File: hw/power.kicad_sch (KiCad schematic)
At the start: 2 parts, among them J1 TYPE-C-31-M-13C

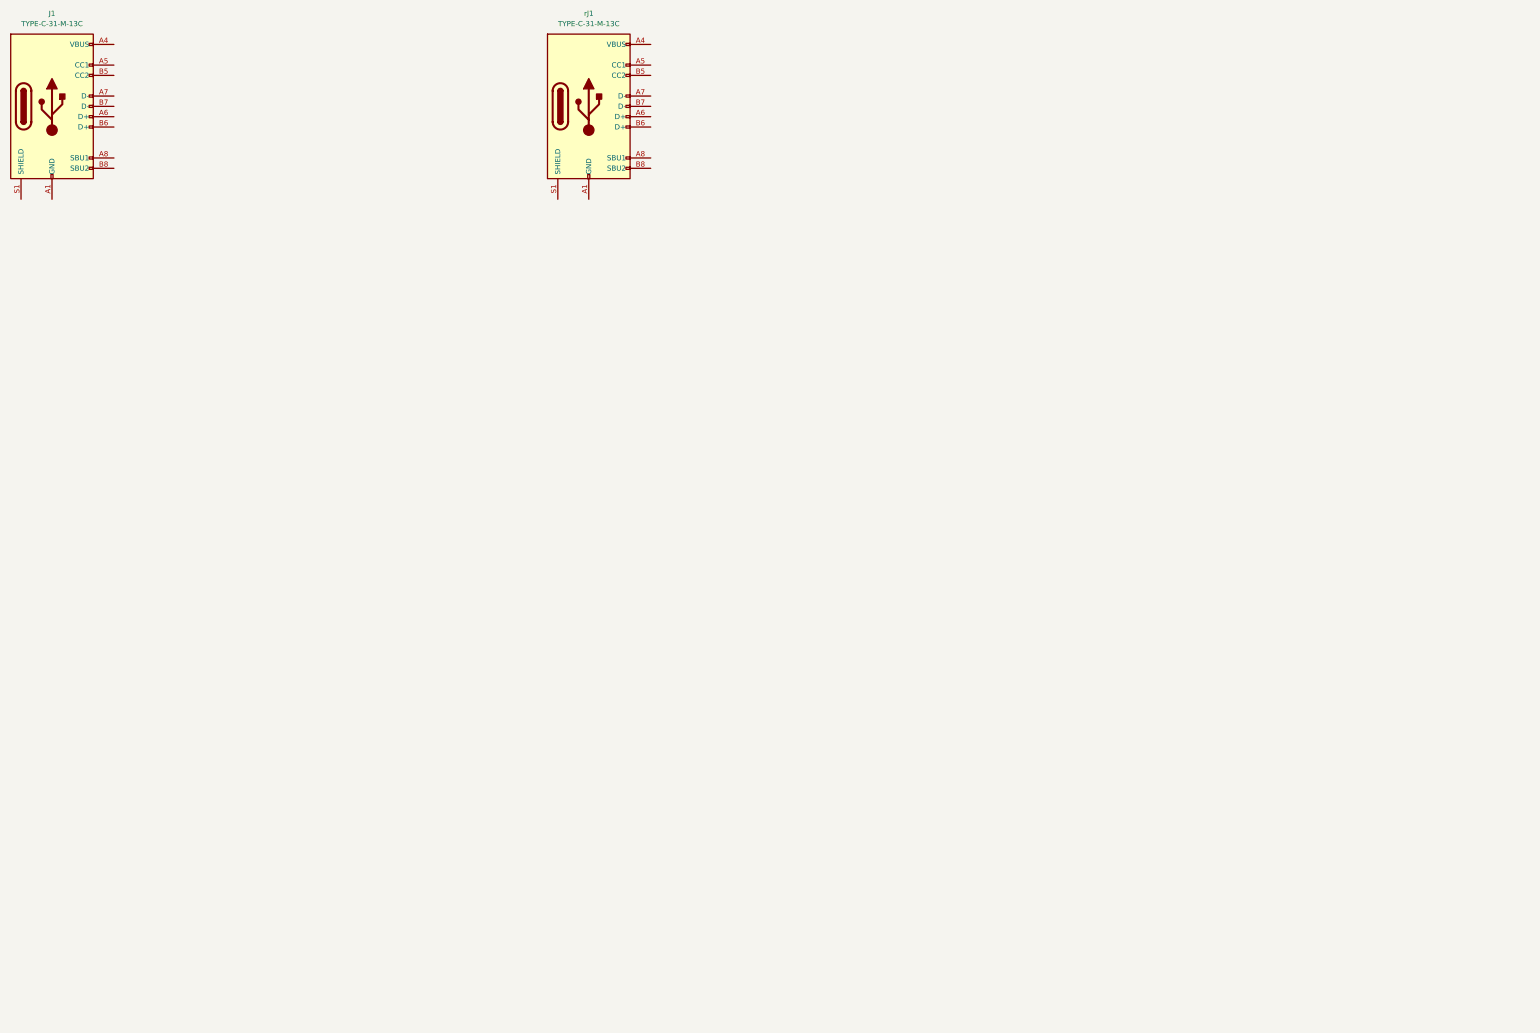
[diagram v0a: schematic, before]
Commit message: Power schematic with npm1100 setup
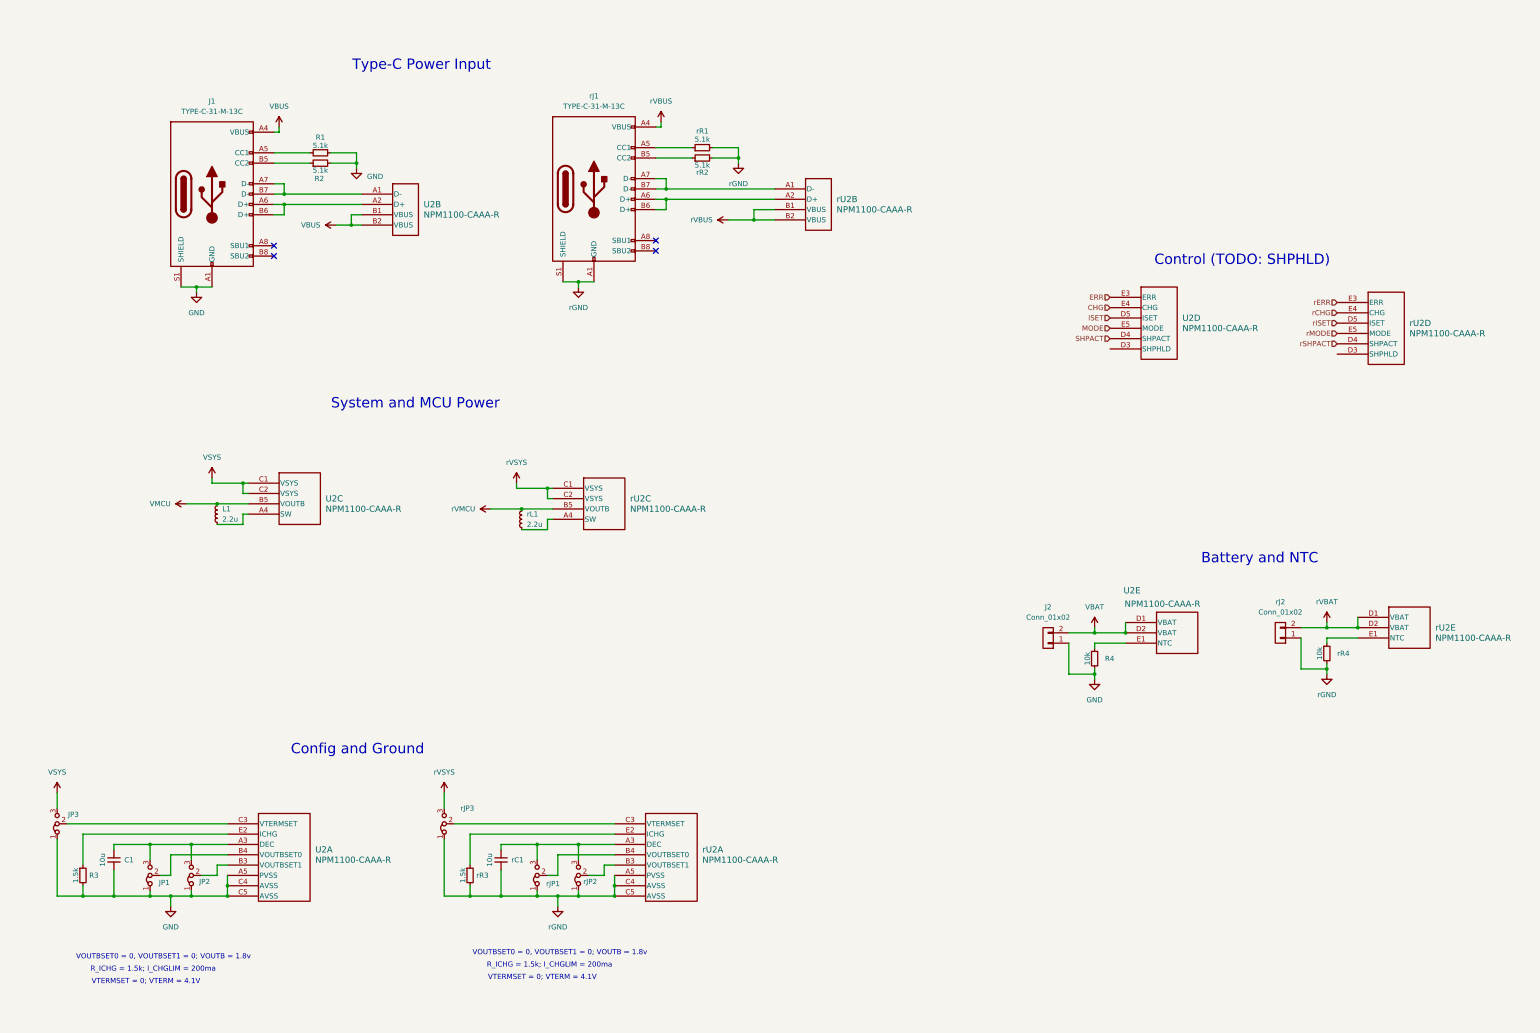
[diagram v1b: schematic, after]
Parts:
- added C1, rC1: 10u, symbol Alidade:C
- added J2, rJ2: Conn_01x02, symbol Alidade:Conn_01x02
- added JP1, JP2, JP3, rJP1, rJP2, rJP3: Jumper_3_Bridged12, symbol Alidade:Jumper_3_Bridged12
- added L1, rL1: 2.2u, symbol Alidade:L
- added R1, R2, rR1, rR2: 5.1k, symbol Alidade:R
- added R3, rR3: 1.5k, symbol Alidade:R
- added R4, rR4: 10k, symbol Alidade:R
- added U2, rU2: NPM1100-CAAA-R, Alidade:WLCSP_2p075X2p075_NOR, symbol Alidade:NPM1100-CAAA-R
- J1, rJ1: symbol Connector:USB_C_Receptacle_USB2.0 -> Alidade:USB_C_Receptacle_USB2.0
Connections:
- net rGND: now reaches rJ1.A1 (GND), rJ1.A12 (GND), rJ1.B1 (GND), rJ1.B12 (GND)
- net rGND: now also rJ1.S1 (SHIELD), rC1.2, rJ2.1 (Pin_1), rJP1.1 (A), rJP2.1 (A), rJP3.1 (A), rR1.2, rR2.2, rR3.2, rR4.2, rU2.A5 (PVSS), rU2.C4 (AVSS), rU2.C5 (AVSS)
- net rVBUS: now reaches rJ1.A4 (VBUS), rJ1.A9 (VBUS), rJ1.B4 (VBUS), rJ1.B9 (VBUS)
- net rVBUS: now also rU2.B1 (VBUS), rU2.B2 (VBUS)
- net at rJ1.A5 (CC1): now also rR1.1
- net at rJ1.A6 (D+): now also rJ1.B6 (D+), rU2.A2 (D+)
- net at rJ1.A7 (D-): now also rJ1.B7 (D-), rU2.A1 (D-)
- net at rJ1.B5 (CC2): now also rR2.1
- net GND: now reaches J1.A1 (GND), J1.A12 (GND), J1.B1 (GND), J1.B12 (GND)
- net GND: now also J1.S1 (SHIELD), C1.2, J2.1 (Pin_1), JP1.1 (A), JP2.1 (A), JP3.1 (A), R1.1, R2.2, R3.2, R4.2, U2.A5 (PVSS), U2.C4 (AVSS), U2.C5 (AVSS)
- net VBUS: now reaches J1.A4 (VBUS), J1.A9 (VBUS), J1.B4 (VBUS), J1.B9 (VBUS)
- net VBUS: now also U2.B1 (VBUS), U2.B2 (VBUS)
- net at J1.A5 (CC1): now also R1.2
- net at J1.A6 (D+): now also J1.B6 (D+), U2.A2 (D+)
- net at J1.A7 (D-): now also J1.B7 (D-), U2.A1 (D-)
- net at J1.B5 (CC2): now also R2.1
- new net: L1.1, U2.A4 (SW)
- new net: R3.1, U2.E2 (ICHG)
- new net: rL1.1, rU2.A4 (SW)
- new net: rC1.1, rJP1.3 (B), rJP2.3 (B), rU2.A3 (DEC)
- new net: rR4.1, rU2.E1 (NTC)
- new net: JP2.2 (C), U2.B3 (VOUTBSET1)
- new net: C1.1, JP1.3 (B), JP2.3 (B), U2.A3 (DEC)
- new net: rJP2.2 (C), rU2.B3 (VOUTBSET1)
- new net: rJP1.2 (C), rU2.B4 (VOUTBSET0)
- new net: rJP3.2 (C), rU2.C3 (VTERMSET)
- new net: rR3.1, rU2.E2 (ICHG)
- new net: R4.1, U2.E1 (NTC)
- new net: JP1.2 (C), U2.B4 (VOUTBSET0)
- new net: JP3.2 (C), U2.C3 (VTERMSET)
- new net CHG: U2.E4 (CHG)
- new net ERR: U2.E3 (ERR)
- new net ISET: U2.D5 (ISET)
- new net MODE: U2.E5 (MODE)
- new net SHPACT: U2.D4 (SHPACT)
- new net VBAT: J2.2 (Pin_2), U2.D1 (VBAT), U2.D2 (VBAT)
- new net VMCU: L1.2, U2.B5 (VOUTB)
- new net VSYS: JP3.3 (B), U2.C1 (VSYS), U2.C2 (VSYS)
- new net rCHG: rU2.E4 (CHG)
- new net rERR: rU2.E3 (ERR)
- new net rISET: rU2.D5 (ISET)
- new net rMODE: rU2.E5 (MODE)
- new net rSHPACT: rU2.D4 (SHPACT)
- new net rVBAT: rJ2.2 (Pin_2), rU2.D1 (VBAT), rU2.D2 (VBAT)
- new net rVMCU: rL1.2, rU2.B5 (VOUTB)
- new net rVSYS: rJP3.3 (B), rU2.C1 (VSYS), rU2.C2 (VSYS)
- no-connect marks 0 -> 4
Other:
- note added: "Battery and NTC"
- note added: "Config and Ground"
- note added: "Control (TODO: SHPHLD)"
- note added: "R_ICHG = 1.5k; I_CHGLIM = 200ma"
- note added: "System and MCU Power"
- note added: "Type-C Power Input"
- note added: "VOUTBSET0 = 0, VOUTBSET1 = 0; VOUTB = 1.8v"
- note added: "VTERMSET = 0; VTERM = 4.1V"

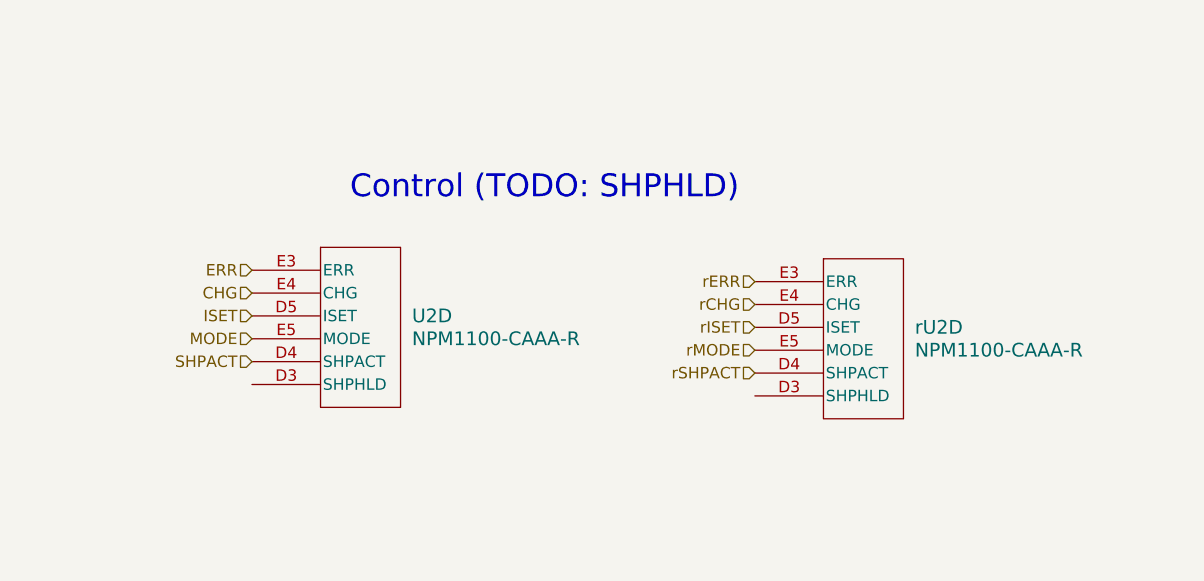
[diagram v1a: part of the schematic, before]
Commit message: Sheet pin directions
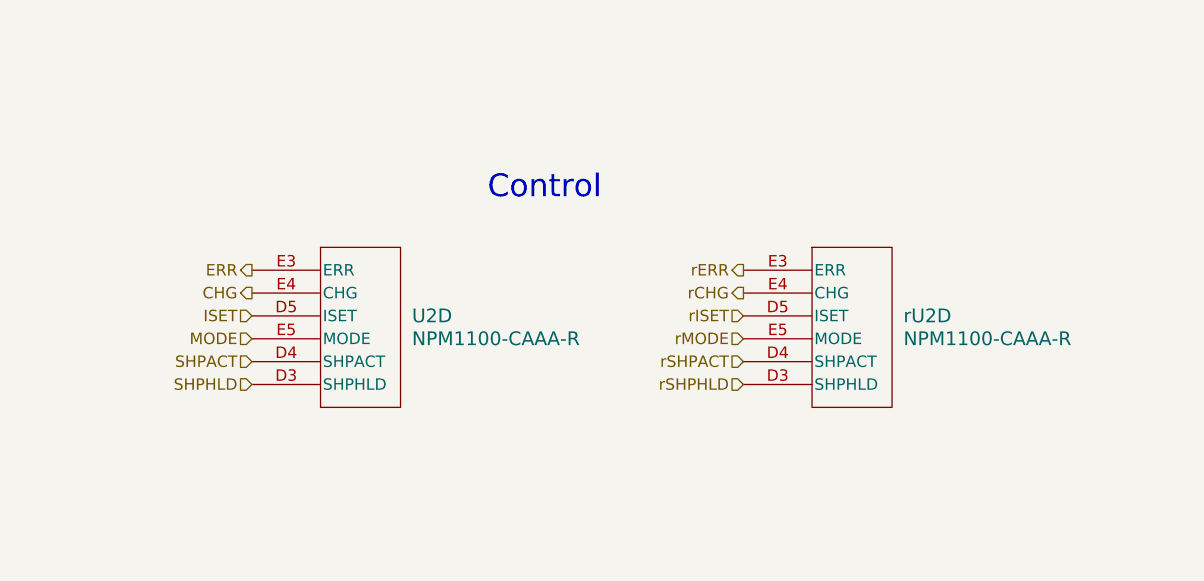
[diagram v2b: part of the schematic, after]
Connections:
- net SHPHLD: now reaches U2.D3 (SHPHLD)
- net rSHPHLD: now reaches rU2.D3 (SHPHLD)
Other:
- note added: "Control"
- note removed: "Control (TODO: SHPHLD)"
- moved on the sheet: rU2D
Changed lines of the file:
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@@
 		)
 	)
-	(text "Control (TODO: SHPHLD)"
+	(text "Control"
 		(exclude_from_sim no)
 		(at 325.882 81.026 0)
@@
 	)
 	(hierarchical_label "ERR"
-		(shape input)
+		(shape output)
 		(at 293.37 90.17 180)
 		(effects
@@
 	(hierarchical_label "rISET"
 		(shape input)
-		(at 349.25 96.52 180)
+		(at 347.98 95.25 180)
 		(effects
 			(font
@@
 	)
 	(hierarchical_label "CHG"
-		(shape input)
+		(shape output)
 		(at 293.37 92.71 180)
 		(effects
@@
 		)
 	)
+	(hierarchical_label "SHPHLD"
+		(shape input)
+		(at 293.37 102.87 180)
+		(effects
+			(font
+				(size 1.27 1.27)
+			)
+			(justify right)
+		)
+	)
 	(hierarchical_label "rCHG"
+		(shape output)
+		(at 347.98 92.71 180)
+		(effects
+			(font
+				(size 1.27 1.27)
+			)
+			(justify right)
+		)
+	)
+	(hierarchical_label "rSHPHLD"
 		(shape input)
-		(at 349.25 93.98 180)
+		(at 347.98 102.87 180)
 		(effects
 			(font
@@
 	)
 	(hierarchical_label "rERR"
-		(shape input)
-		(at 349.25 91.44 180)
+		(shape output)
+		(at 347.98 90.17 180)
 		(effects
 			(font
@@
 	(hierarchical_label "rSHPACT"
 		(shape input)
-		(at 349.25 101.6 180)
+		(at 347.98 100.33 180)
 		(effects
 			(font
@@
 	(hierarchical_label "rMODE"
 		(shape input)
-		(at 349.25 99.06 180)
+		(at 347.98 97.79 180)
 		(effects
 			(font
@@
 	(symbol
 		(lib_id "Alidade:NPM1100-CAAA-R")
-		(at 349.25 88.9 0)
+		(at 347.98 87.63 0)
 		(unit 4)
 		(exclude_from_sim no)
@@
 		(fields_autoplaced yes)
 		(property "Reference" "rU2"
-			(at 367.03 96.5199 0)
+			(at 365.76 95.2499 0)
 			(effects
 				(font
@@
 		)
 		(property "Value" "NPM1100-CAAA-R"
-			(at 367.03 99.0599 0)
+			(at 365.76 97.7899 0)
 			(effects
 				(font
@@
 		)
 		(property "Footprint" "Alidade:WLCSP_2p075X2p075_NOR"
-			(at 362.966 106.934 0)
+			(at 361.696 105.664 0)
 			(effects
 				(font
@@
 		)
 		(property "Datasheet" "NPM1100-CAAA-R"
-			(at 362.712 110.49 0)
+			(at 361.442 109.22 0)
 			(effects
 				(font
@@
 		)
 		(property "Description" ""
-			(at 349.25 88.9 0)
+			(at 347.98 87.63 0)
 			(effects
 				(font

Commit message: Battery Monitor
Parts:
- added Q1, rQ1: DMC2400UV, symbol Alidade:DMC2400UV
- added R5, R6, rR5, rR6: 1M, symbol Alidade:R
- added R7, rR7: 1.5M, symbol Alidade:R
- added R8, rR8: 220k, symbol Alidade:R
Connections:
- net GND: now also Q1.4 (D), R6.2, R8.2
- net VBAT: now also Q1.6 (S), R5.1
- net rGND: now also rQ1.4 (D), rR6.2, rR8.2
- net rVBAT: now also rQ1.6 (S), rR5.1
- new net: rQ1.3 (D), rR7.1
- new net: rQ1.1 (S), rQ1.5 (G), rR5.2
- new net: Q1.3 (D), R7.1
- new net: Q1.1 (S), Q1.5 (G), R5.2
- new net BATMON: R7.2, R8.1
- new net BATMONEN: Q1.2 (G), R6.1
- new net rBATMON: rR7.2, rR8.1
- new net rBATMONEN: rQ1.2 (G), rR6.1
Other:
- note added: "Battery Monitor"
- moved on the sheet: J2, R4, U2D, U2E, rJ2, rR4, rU2D, rU2E

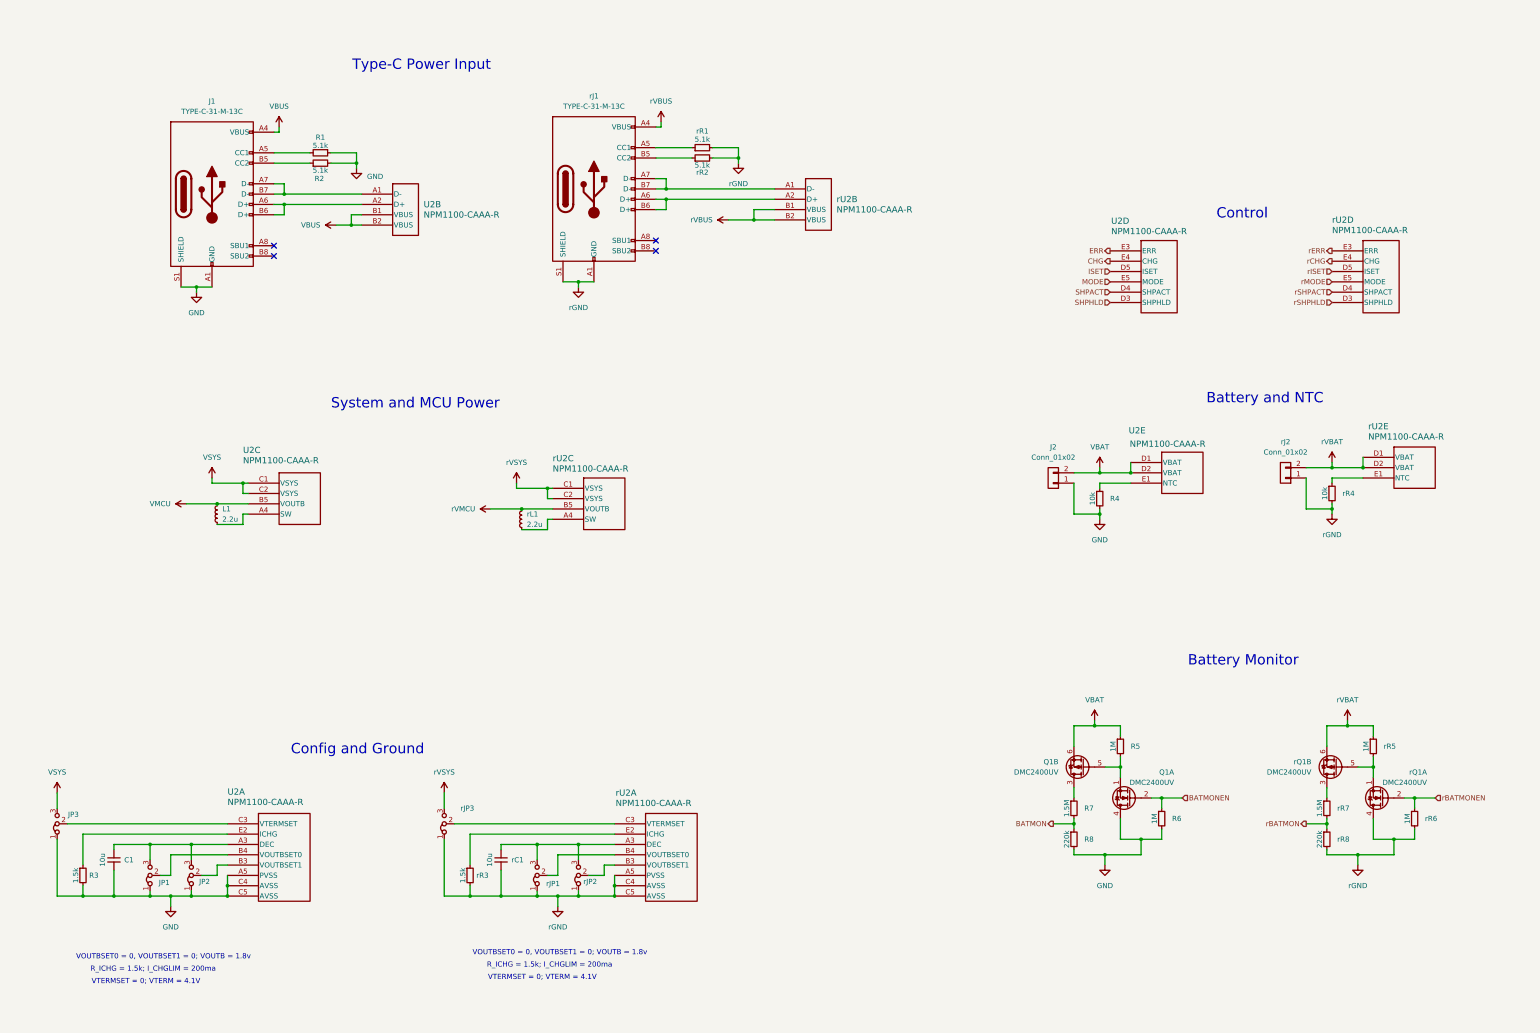
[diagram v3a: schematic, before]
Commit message: Decoupling caps
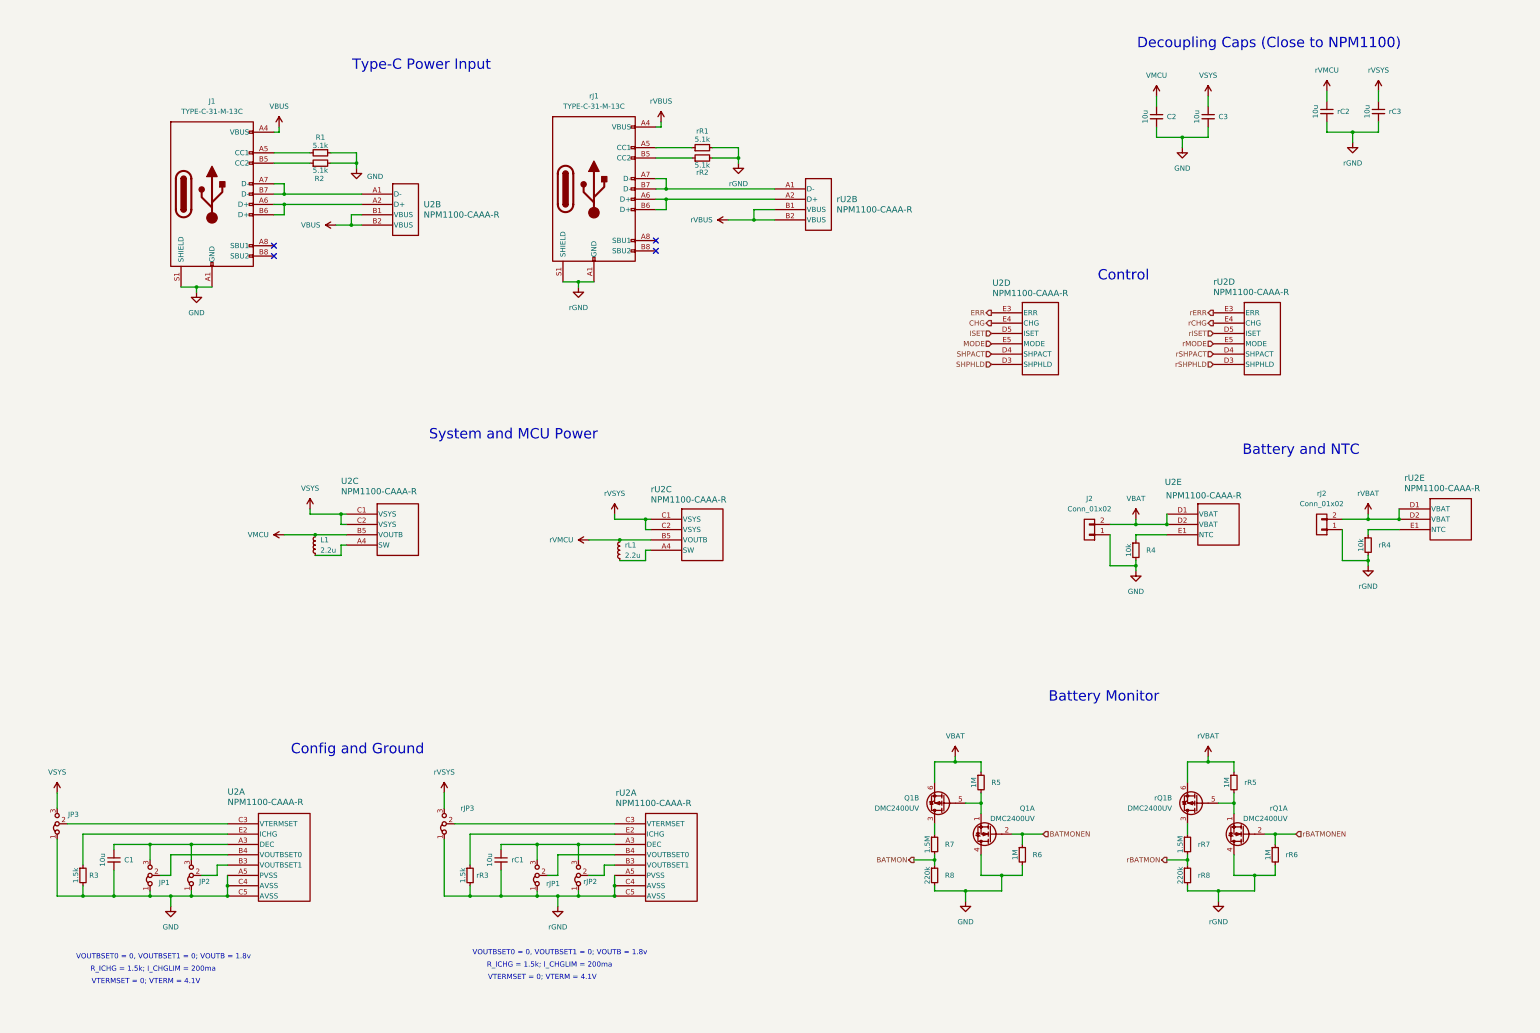
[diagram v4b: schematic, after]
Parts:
- added C2, C3, rC2, rC3: 10u, symbol Alidade:C
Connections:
- net GND: now also C2.2, C3.2
- net VMCU: now also C2.1
- net VSYS: now also C3.1
- net rGND: now also rC2.2, rC3.2
- net rVMCU: now also rC2.1
- net rVSYS: now also rC3.1
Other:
- note added: "Decoupling Caps (Close to NPM1100)"
- moved on the sheet: J2, L1, Q1A, Q1B, R4, R5, R6, R7, R8, U2C, U2D, U2E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
